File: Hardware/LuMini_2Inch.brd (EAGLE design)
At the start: 54.1 x 54.1 mm, 57 parts, among them J1 DOUBLE_LED_PAD, J2 DOUBLE_LED_PAD, J3 DOUBLE_LED_PAD

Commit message: adding silk
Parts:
- added LOGO1: OSHW-LOGOS, SparkFun-Aesthetics:OSHW-LOGO-S
- added LOGO2: SFE_LOGO_NAME.1_INCH, SparkFun-Aesthetics:SFE_LOGO_NAME_.1
- added U$12: (no value), buzzard_labels (5):258
- added U$13: (no value), buzzard_labels (5):3510
- added U$2: (no value), buzzard_labels (5):54
- added U$3: (no value), buzzard_labels (5):156
- added U$6: (no value), buzzard_labels (6):194
- moved U$1 49.8 mm to (24.7, 3.40), turned to 180 degrees
- moved U$11 48.4 mm to (21.3, 4.80), turned to 180 degrees
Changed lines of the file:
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@@
 <grid distance="0.05" unitdist="inch" unit="inch" style="lines" multiple="1" display="yes" altdistance="0.0005" altunitdist="inch" altunit="inch"/>
 <layers>
-<layer number="1" name="Top" color="4" fill="1" visible="yes" active="yes"/>
+<layer number="1" name="Top" color="4" fill="1" visible="no" active="yes"/>
 <layer number="2" name="Route2" color="16" fill="1" visible="no" active="no"/>
 <layer number="15" name="Route15" color="23" fill="1" visible="no" active="no"/>
@@
 <layer number="19" name="Unrouted" color="6" fill="1" visible="yes" active="yes"/>
 <layer number="20" name="Dimension" color="24" fill="1" visible="yes" active="yes"/>
-<layer number="21" name="tPlace" color="7" fill="1" visible="yes" active="yes"/>
+<layer number="21" name="tPlace" color="16" fill="1" visible="yes" active="yes"/>
 <layer number="22" name="bPlace" color="7" fill="1" visible="yes" active="yes"/>
 <layer number="23" name="tOrigins" color="15" fill="1" visible="yes" active="yes"/>
@@
 <element name="J1" library="Andy" package="DOUBLELEDPAD" value="DOUBLE_LED_PAD" x="52.5018" y="31.8135" rot="MR261"/>
 <element name="J2" library="Andy" package="DOUBLELEDPAD" value="DOUBLE_LED_PAD" x="52.832" y="27.9527" rot="MR270"/>
-<element name="U$1" library="buzzard_labels (2)" package="LUMINI0" value="" x="31.1785" y="52.7685" rot="MR0"/>
+<element name="U$1" library="buzzard_labels (2)" package="LUMINI0" value="" x="24.7015" y="3.4036" rot="MR180"/>
 <element name="U$4" library="buzzard_labels (25)" package="5V6" value="" x="50.673" y="31.9405" rot="MR262"/>
 <element name="U$5" library="buzzard_labels (25)" package="G4" value="" x="50.3555" y="33.655" rot="MR262"/>
@@
 </element>
 <element name="J3" library="Andy" package="DOUBLELEDPAD" value="DOUBLE_LED_PAD" x="52.5272" y="23.876" rot="MR99"/>
-<element name="U$11" library="buzzard_labels (28)" package="40_APA102_LED#S1" value="" x="34.6075" y="51.3715" rot="MR0"/>
+<element name="U$11" library="buzzard_labels (28)" package="40_APA102_LED#S1" value="" x="21.2725" y="4.8006" rot="MR180"/>
 <element name="H1" library="SparkFun-Hardware" package="STANDOFF-ELECTRICAL-NOTHERMALS" value="STANDOFF_ELECTRICALSTANDOFF-ELECTRICAL-NOTHERMALS" x="10.16" y="27.94"/>
 <element name="H2" library="SparkFun-Hardware" package="STANDOFF-ELECTRICAL-NOTHERMALS" value="STANDOFF_ELECTRICALSTANDOFF-ELECTRICAL-NOTHERMALS" x="45.72" y="27.94"/>
@@
 <attribute name="PROD_ID" value="CAP-08280" x="49.784" y="19.939" size="1.778" layer="28" font="vector" rot="MR110" display="off"/>
 </element>
+<element name="LOGO1" library="SparkFun-Aesthetics" package="OSHW-LOGO-S" value="OSHW-LOGOS" x="3.175" y="27.9527" rot="MR270"/>
+<element name="LOGO2" library="SparkFun-Aesthetics" package="SFE_LOGO_NAME_.1" value="SFE_LOGO_NAME.1_INCH" x="27.94" y="52.07" rot="MR0"/>
+<element name="U$2" library="buzzard_labels (5)" package="54" value="" x="46.4947" y="44.4119" rot="MR45"/>
+<element name="U$3" library="buzzard_labels (5)" package="156" value="" x="11.5062" y="46.5328" rot="MR315"/>
+<element name="U$6" library="buzzard_labels (6)" package="194" value="" x="3.6957" y="33.3629" rot="MR279"/>
+<element name="U$12" library="buzzard_labels (5)" package="258" value="" x="9.1948" y="11.6713" rot="MR225"/>
+<element name="U$13" library="buzzard_labels (5)" package="3510" value="" x="44.2468" y="9.2456" rot="MR135"/>
 </elements>
 <signals>

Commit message: post checklist
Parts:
- added FD1, FD2, FD3, FD4: FIDUCIALUFIDUCIAL, SparkFun-Aesthetics:FIDUCIAL-MICRO
- added H5, H6, H7, H8: STANDOFF_ELECTRICALSTANDOFF-ELECTRICAL-NOTHERMALS, SparkFun-Hardware:STANDOFF-ELECTRICAL-NOTHERMALS
- added U$14: (no value), SparkFun-Aesthetics:ORDERING_INSTRUCTIONS
- C1: value 4.7uF -> DNP; device SparkFun-Capacitors:0603 -> SparkFun-Capacitors:1206
- U$1: device buzzard_labels (2):LUMINI0 -> buzzard_labels (8):LUMINI_2#0
- moved H2 1.27 mm to (47.0, 27.9)
- moved H3 1.27 mm to (27.9, 47.0)
- moved H1 1.27 mm to (8.89, 27.9)
- moved H4 1.27 mm to (27.9, 8.89)
- moved U$1 0.89 mm to (23.8, 3.40)
- moved C1 0.67 mm to (50.0, 19.3)
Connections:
- net GND: now also H5.P1, H6.P1, H7.P1, H8.P1
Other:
- board size 54.1 x 54.1 mm -> 54.2 x 54.2 mm
- board text added: "Black PCB 2 Oz. Cu"

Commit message: cleaning schematic
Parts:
- H1, H2, H3, H4, H5, H6, H7, H8: value STANDOFF_ELECTRICALSTANDOFF-ELECTRICAL-NOTHERMALS -> STANDOFF_ELECTRICAL-NOTHERMALS
- J1, J2, J3: value DOUBLE_LED_PAD -> SOLDER_PAD_2; device Andy:DOUBLELEDPAD -> SparkFun-Connectors:SOLDER_PAD_2
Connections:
- net N$133 renamed CO
- net N$134 renamed DO
- net N$2 renamed CI
- net N$3 renamed DI
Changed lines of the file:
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@@
 <dimension x1="27.94" y1="54.991" x2="27.94" y2="0.889" x3="63.5" y3="27.94" textsize="2.54" layer="47" dtype="diameter" unit="inch"/>
 <circle x="27.94" y="27.94" radius="22.225" width="0.2032" layer="21"/>
-<dimension x1="27.94" y1="50.165" x2="27.94" y2="5.715" x3="59.69" y3="27.94" textsize="2.54" layer="21" dtype="diameter" unit="inch"/>
-<dimension x1="27.94" y1="46.99" x2="27.94" y2="8.89" x3="35.56" y3="27.94" textsize="2.54" layer="21" unit="inch"/>
-<dimension x1="8.89" y1="27.94" x2="27.94" y2="8.89" x3="22.225" y3="22.225" textsize="2.54" layer="21" unit="inch"/>
-<dimension x1="49.53" y1="49.53" x2="49.53" y2="6.35" x3="67.31" y3="27.94" textsize="2.54" layer="21" unit="inch"/>
-<dimension x1="6.35" y1="49.53" x2="49.53" y2="6.35" x3="61.595" y3="61.595" textsize="2.54" layer="21" unit="inch"/>
+<dimension x1="27.94" y1="50.165" x2="27.94" y2="5.715" x3="59.69" y3="27.94" textsize="2.54" layer="47" dtype="diameter" unit="inch"/>
+<dimension x1="27.94" y1="46.99" x2="27.94" y2="8.89" x3="35.56" y3="27.94" textsize="2.54" layer="47" unit="inch"/>
+<dimension x1="8.89" y1="27.94" x2="27.94" y2="8.89" x3="22.225" y3="22.225" textsize="2.54" layer="47" unit="inch"/>
+<dimension x1="49.53" y1="49.53" x2="49.53" y2="6.35" x3="67.31" y3="27.94" textsize="2.54" layer="47" unit="inch"/>
+<dimension x1="6.35" y1="49.53" x2="49.53" y2="6.35" x3="61.595" y3="61.595" textsize="2.54" layer="47" unit="inch"/>
 </plain>
 <attributes>
@@
 <attribute name="PROD_ID" value="DIO-13883" x="15.6257" y="40.317709375" size="1.778" layer="27" rot="R261" display="off"/>
 </element>
-<element name="J1" library="Andy" package="DOUBLELEDPAD" value="DOUBLE_LED_PAD" x="52.5018" y="31.8135" rot="MR261"/>
-<element name="J2" library="Andy" package="DOUBLELEDPAD" value="DOUBLE_LED_PAD" x="52.832" y="27.9527" rot="MR270"/>
+<element name="J1" library="SparkFun-Connectors" package="SOLDER_PAD_2" value="SOLDER_PAD_2" x="52.5018" y="31.8135" rot="MR261"/>
+<element name="J2" library="SparkFun-Connectors" package="SOLDER_PAD_2" value="SOLDER_PAD_2" x="52.832" y="27.9527" rot="MR270"/>
 <element name="U$1" library="buzzard_labels (8)" package="LUMINI_2#0" value="" x="23.8125" y="3.4036" rot="MR180"/>
 <element name="U$4" library="buzzard_labels (25)" package="5V6" value="" x="50.673" y="31.9405" rot="MR262"/>
@@
 <attribute name="PROD_ID" value="DIO-13883" x="38.033153125" y="1.5385" size="1.778" layer="27" rot="R81" display="off"/>
 </element>
-<element name="J3" library="Andy" package="DOUBLELEDPAD" value="DOUBLE_LED_PAD" x="52.5272" y="23.876" rot="MR99"/>
+<element name="J3" library="SparkFun-Connectors" package="SOLDER_PAD_2" value="SOLDER_PAD_2" x="52.5272" y="23.876" rot="MR99"/>
 <element name="U$11" library="buzzard_labels (28)" package="40_APA102_LED#S1" value="" x="21.2725" y="4.8006" rot="MR180"/>
-<element name="H1" library="SparkFun-Hardware" package="STANDOFF-ELECTRICAL-NOTHERMALS" value="STANDOFF_ELECTRICALSTANDOFF-ELECTRICAL-NOTHERMALS" x="8.89" y="27.94"/>
-<element name="H2" library="SparkFun-Hardware" package="STANDOFF-ELECTRICAL-NOTHERMALS" value="STANDOFF_ELECTRICALSTANDOFF-ELECTRICAL-NOTHERMALS" x="46.99" y="27.94"/>
-<element name="H3" library="SparkFun-Hardware" package="STANDOFF-ELECTRICAL-NOTHERMALS" value="STANDOFF_ELECTRICALSTANDOFF-ELECTRICAL-NOTHERMALS" x="27.94" y="46.99"/>
-<element name="H4" library="SparkFun-Hardware" package="STANDOFF-ELECTRICAL-NOTHERMALS" value="STANDOFF_ELECTRICALSTANDOFF-ELECTRICAL-NOTHERMALS" x="27.94" y="8.89"/>
+<element name="H1" library="SparkFun-Hardware" package="STANDOFF-ELECTRICAL-NOTHERMALS" value="STANDOFF_ELECTRICAL-NOTHERMALS" x="8.89" y="27.94"/>
+<element name="H2" library="SparkFun-Hardware" package="STANDOFF-ELECTRICAL-NOTHERMALS" value="STANDOFF_ELECTRICAL-NOTHERMALS" x="46.99" y="27.94"/>
+<element name="H3" library="SparkFun-Hardware" package="STANDOFF-ELECTRICAL-NOTHERMALS" value="STANDOFF_ELECTRICAL-NOTHERMALS" x="27.94" y="46.99"/>
+<element name="H4" library="SparkFun-Hardware" package="STANDOFF-ELECTRICAL-NOTHERMALS" value="STANDOFF_ELECTRICAL-NOTHERMALS" x="27.94" y="8.89"/>
 <element name="C1" library="SparkFun-Capacitors" package="1206" value="DNP" x="49.9618" y="19.2913" rot="MR110">
 <attribute name="PROD_ID" value="CAP-10300" x="49.9618" y="19.2913" size="1.778" layer="28" font="vector" rot="MR110" display="off"/>
@@
 <element name="U$12" library="buzzard_labels (5)" package="258" value="" x="9.1948" y="11.6713" rot="MR225"/>
 <element name="U$13" library="buzzard_labels (5)" package="3510" value="" x="44.2468" y="9.2456" rot="MR135"/>
-<element name="H5" library="SparkFun-Hardware" package="STANDOFF-ELECTRICAL-NOTHERMALS" value="STANDOFF_ELECTRICALSTANDOFF-ELECTRICAL-NOTHERMALS" x="6.35" y="6.35"/>
-<element name="H6" library="SparkFun-Hardware" package="STANDOFF-ELECTRICAL-NOTHERMALS" value="STANDOFF_ELECTRICALSTANDOFF-ELECTRICAL-NOTHERMALS" x="6.35" y="49.53"/>
-<element name="H7" library="SparkFun-Hardware" package="STANDOFF-ELECTRICAL-NOTHERMALS" value="STANDOFF_ELECTRICALSTANDOFF-ELECTRICAL-NOTHERMALS" x="49.53" y="6.35"/>
-<element name="H8" library="SparkFun-Hardware" package="STANDOFF-ELECTRICAL-NOTHERMALS" value="STANDOFF_ELECTRICALSTANDOFF-ELECTRICAL-NOTHERMALS" x="49.53" y="49.53"/>
+<element name="H5" library="SparkFun-Hardware" package="STANDOFF-ELECTRICAL-NOTHERMALS" value="STANDOFF_ELECTRICAL-NOTHERMALS" x="6.35" y="6.35"/>
+<element name="H6" library="SparkFun-Hardware" package="STANDOFF-ELECTRICAL-NOTHERMALS" value="STANDOFF_ELECTRICAL-NOTHERMALS" x="6.35" y="49.53"/>
+<element name="H7" library="SparkFun-Hardware" package="STANDOFF-ELECTRICAL-NOTHERMALS" value="STANDOFF_ELECTRICAL-NOTHERMALS" x="49.53" y="6.35"/>
+<element name="H8" library="SparkFun-Hardware" package="STANDOFF-ELECTRICAL-NOTHERMALS" value="STANDOFF_ELECTRICAL-NOTHERMALS" x="49.53" y="49.53"/>
 <element name="FD1" library="SparkFun-Aesthetics" package="FIDUCIAL-MICRO" value="FIDUCIALUFIDUCIAL" x="6.35" y="10.16"/>
 <element name="FD2" library="SparkFun-Aesthetics" package="FIDUCIAL-MICRO" value="FIDUCIALUFIDUCIAL" x="6.35" y="10.16" rot="MR0"/>
@@
 <wire x1="24.7681875" y1="2.556678125" x2="25.871609375" y2="2.298278125" width="0.2032" layer="1"/>
 </signal>
-<signal name="N$2">
+<signal name="CI">
 <contactref element="D1" pad="CKI"/>
 <contactref element="J2" pad="P$2"/>
@@
 <wire x1="50.9778" y1="26.4668" x2="50.9397" y2="26.5049" width="0.1778" layer="1"/>
 </signal>
-<signal name="N$3">
+<signal name="DI">
 <contactref element="D1" pad="SDI"/>
 <contactref element="J2" pad="P$1"/>
@@
 <wire x1="32.665734375" y1="3.61276875" x2="34.777" y2="4.131534375" width="0.2032" layer="1"/>
 </signal>
-<signal name="N$133">
+<signal name="CO">
 <contactref element="D40" pad="CKO"/>
 <contactref element="J3" pad="P$2"/>
@@
 <wire x1="52.578" y1="25.4" x2="52.53316875" y2="24.893334375" width="0.1778" layer="1"/>
 </signal>
-<signal name="N$134">
+<signal name="DO">
 <contactref element="D40" pad="SDO"/>
 <contactref element="J3" pad="P$1"/>

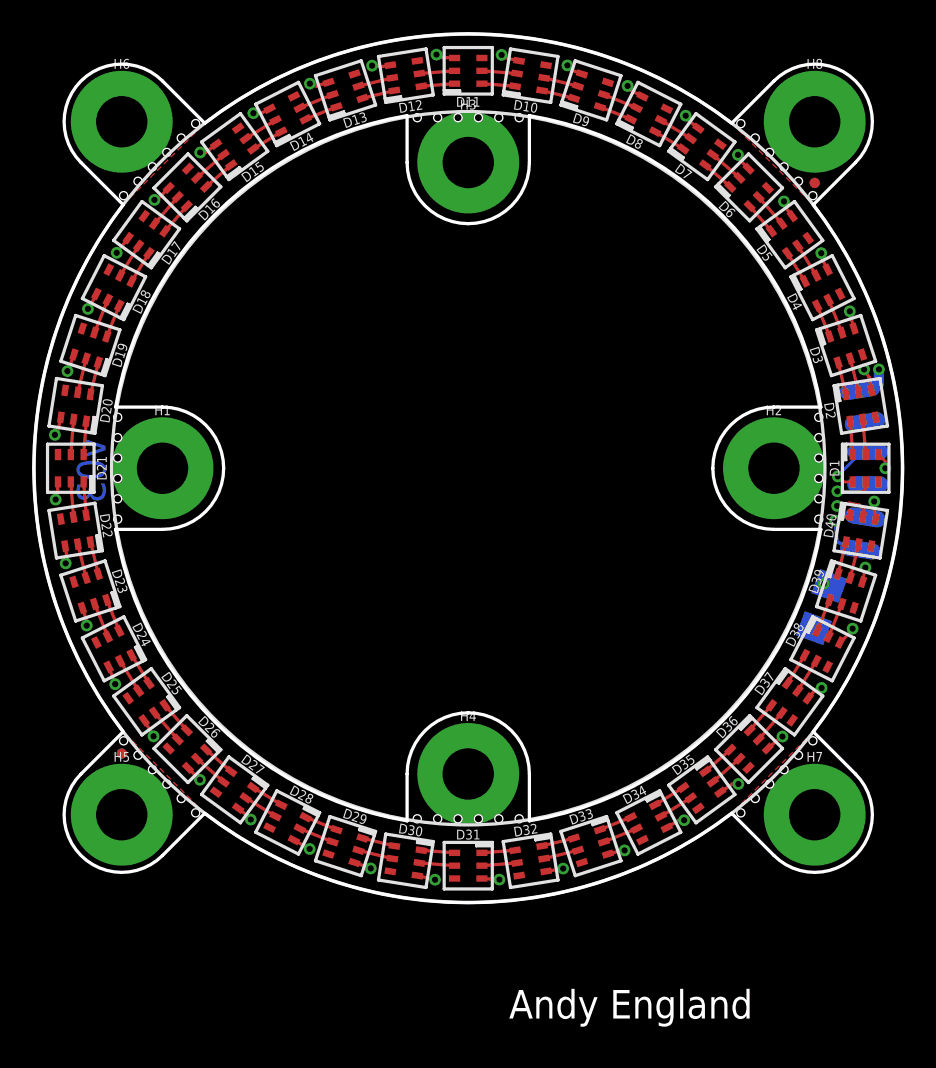
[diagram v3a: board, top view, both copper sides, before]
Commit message: Updating to proper footprint
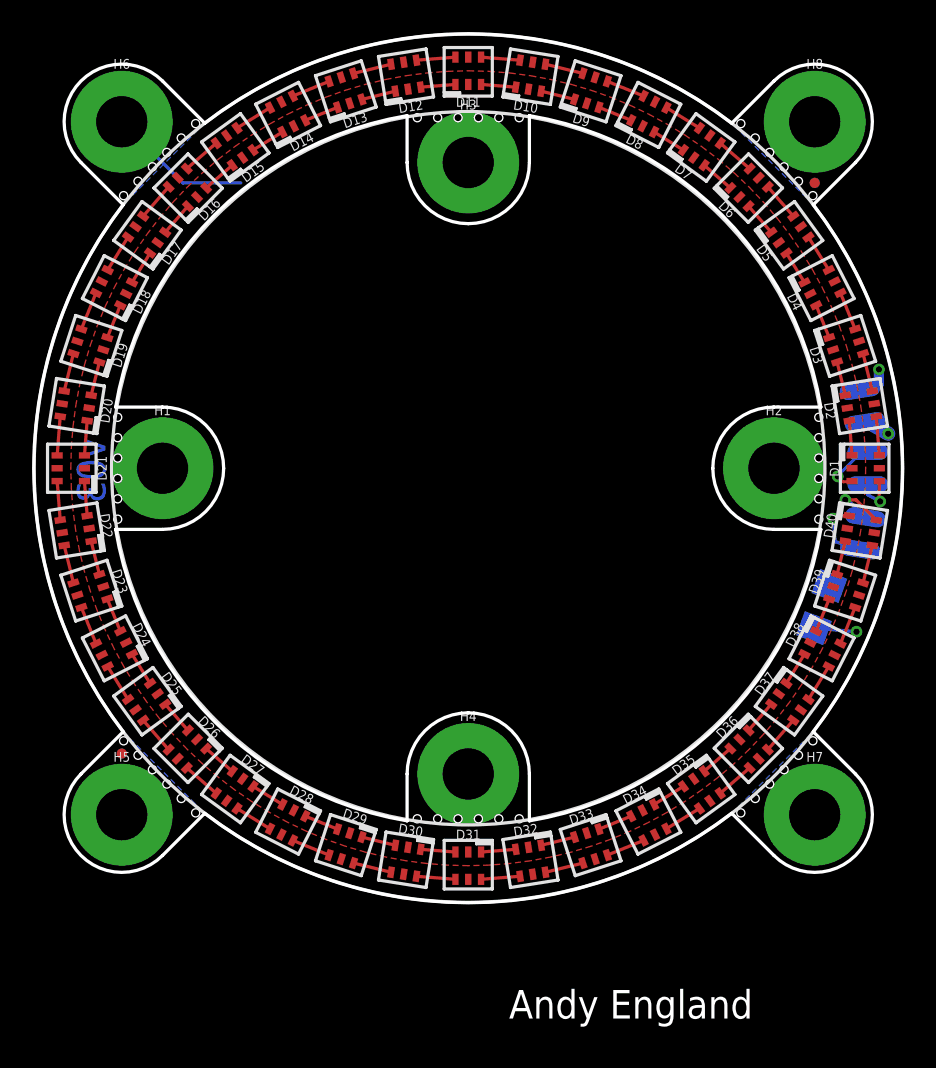
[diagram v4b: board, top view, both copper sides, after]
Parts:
- D1, D10, D11, D12, D13, D14, D15, D16, D17, D18, D19, D2, D20, D21, D22, D23, D24, D25, D26, D27, D28, D29, D3, D30, D31, D32, D33, D34, D35, D36, D37, D38, D39, D4, D40, D5, D6, D7, D8, D9: value APA1022020 -> APA102-2020
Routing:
- net 5V: track 45.6 -> 4.30 mm, vias 40 -> 2
- net GND: track 2.62 -> 11.6 mm, vias 2 -> 1
- net CI: track 4.36 -> 2.82 mm
- added copper zone on layer 1, net 5V
- added copper zone on layer 16, net GND
- removed copper zone on layer 16, net 5V

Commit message: version number change
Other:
- board text added: "v10"
- board text removed: "v03"
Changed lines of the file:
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@@
 <plain>
 <circle x="27.94" y="27.94" radius="27.051" width="0.2032" layer="21"/>
-<text x="5.334" y="29.845" size="1.778" layer="16" font="vector" ratio="15" rot="SMR270">v03</text>
+<text x="5.334" y="29.845" size="1.778" layer="16" font="vector" ratio="15" rot="SMR270">v10</text>
 <hole x="49.784" y="27.305" drill="0.508"/>
 <wire x1="5.969" y1="31.75" x2="8.89" y2="31.75" width="0.2032" layer="20"/>
